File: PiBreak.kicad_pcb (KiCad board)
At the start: 2 copper layers, 56 x 62.9 mm, 317 parts, among them P1 RASPBERRY_PI_P1, P2 CONN_17, P3 CONN_8, P4 CONN_8, P5 CONN_8

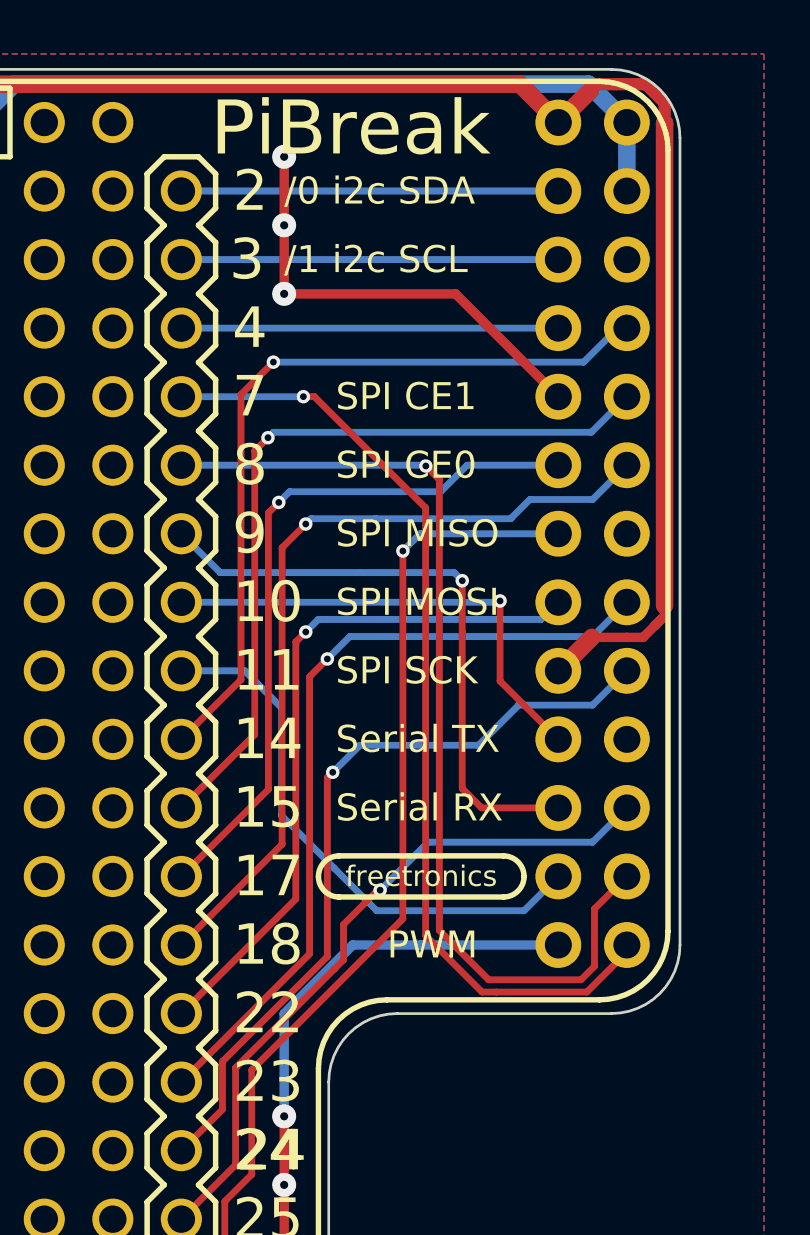
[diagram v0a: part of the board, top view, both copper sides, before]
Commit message: Add 4x2 header for P5 pins
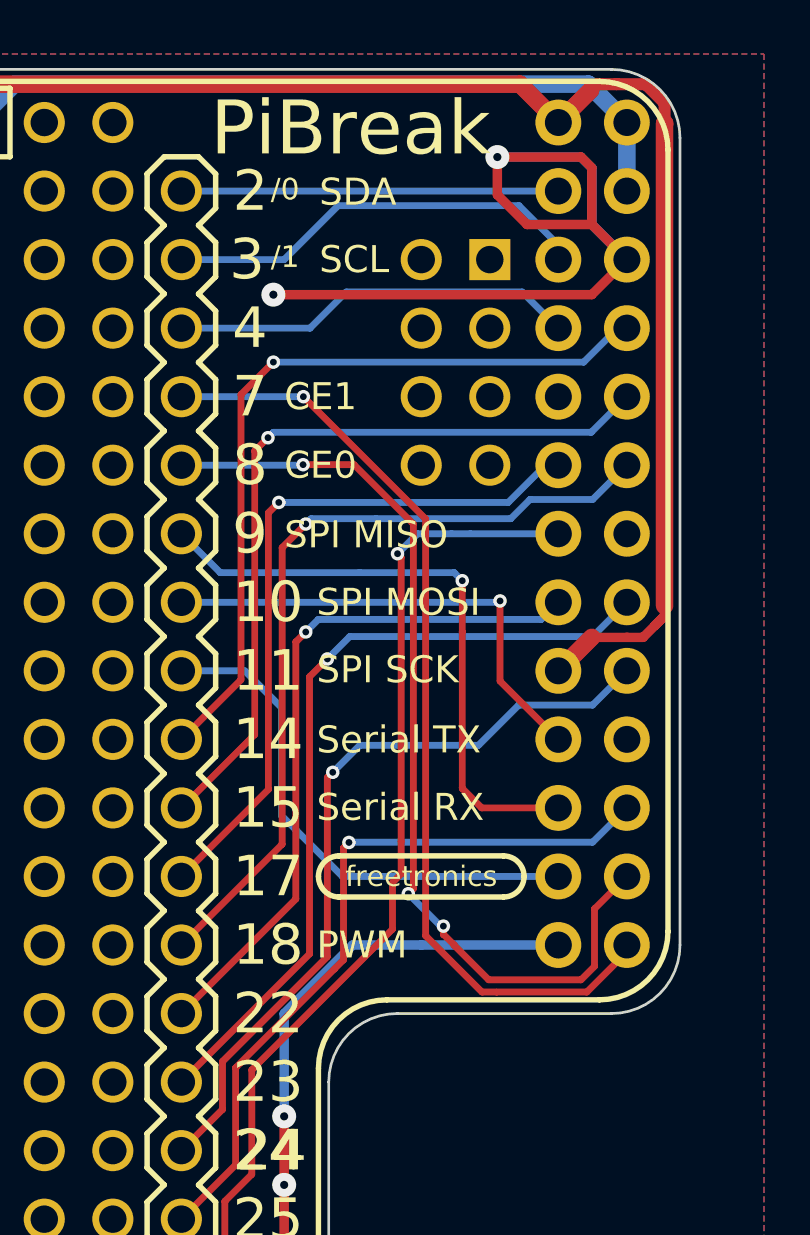
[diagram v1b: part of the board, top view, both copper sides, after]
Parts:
- added P6: CONN_4X2, pin_array_4x2, B.Cu at (260.4, 105.4)
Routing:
- net GND: track 36.9 -> 54.3 mm, vias 6 -> 5
- net /GPIO3_SCL: track 14.0 -> 15.9 mm
- net /GPIO25: track 25.7 -> 27.4 mm
- net /GPIO8_CE0: track 37.0 -> 35.7 mm, vias 1 -> 3
- net /GPIO4_GPCLK0: track 14.0 -> 15.1 mm
- net /GPIO11_SCK: track 20.5 -> 19.5 mm
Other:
- board text added: "/0"
- board text added: "/1"
- board text added: "1"
- board text added: "CE0"
- board text added: "CE1"
- board text added: "SCL"
- board text added: "SDA"
- board text added: "V1.1 SKU: PIBR"
- board text added: "tron.cc/pibr"
- board text removed: "/0 i2c SDA"
- board text removed: "/1 i2c SCL"
- board text removed: "SPI CE0"
- board text removed: "SPI CE1"
- board text removed: "V1.0 SKU: PIBR"
- board text removed: "freetronics.com/pibreak"

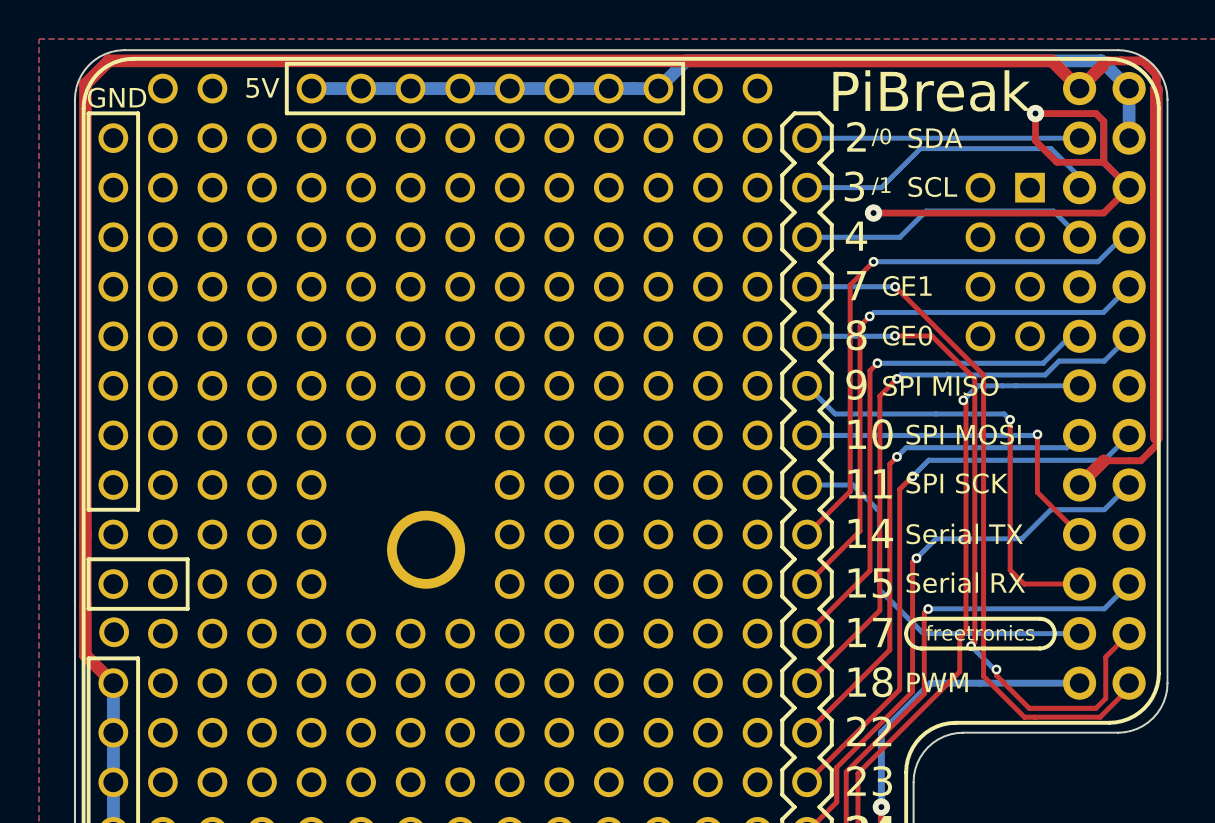
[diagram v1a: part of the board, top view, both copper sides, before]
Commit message: Move reset pins as they were slightly misaligned, bump version to V1.2
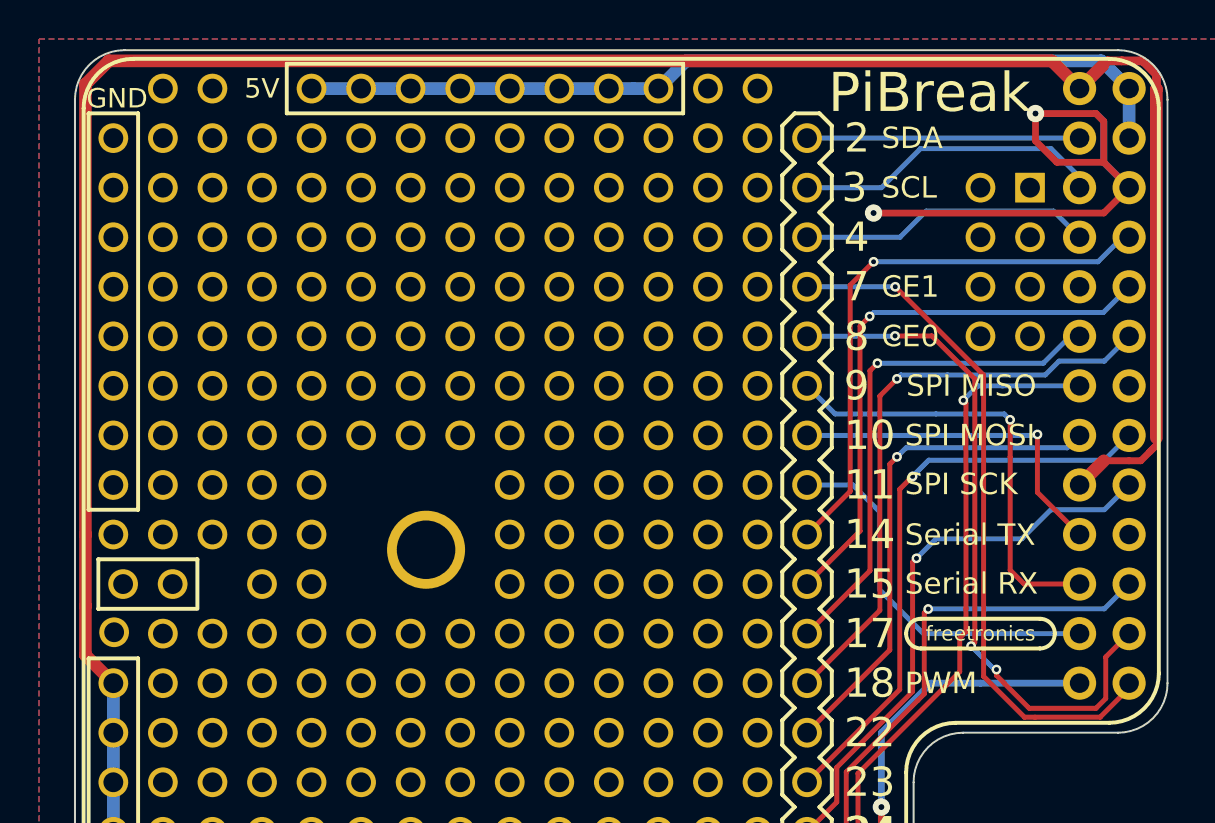
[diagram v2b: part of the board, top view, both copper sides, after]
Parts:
- removed the 1pin_prototyping at (219.7, 121.9)
- moved 1pin_prototyping 0.50 mm to (217.7, 121.9)
- moved 1pin_prototyping 0.50 mm to (215.1, 121.9)
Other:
- rule pad_to_mask_clearance: 0 -> 0.05
- board text added: "V1.2 SKU: PIBR"
- board text removed: "/0"
- board text removed: "/1"
- board text removed: "V1.1 SKU: PIBR"
